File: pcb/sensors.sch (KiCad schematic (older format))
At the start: 2 parts

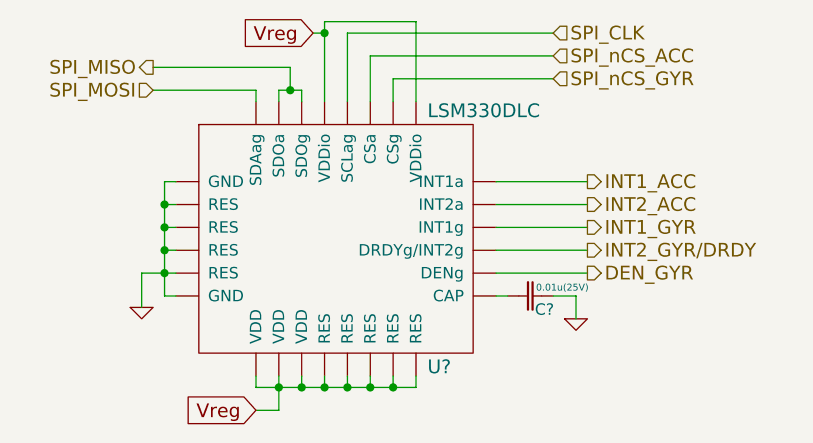
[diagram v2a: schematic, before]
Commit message: Rearranged all the lines except for the power lines.
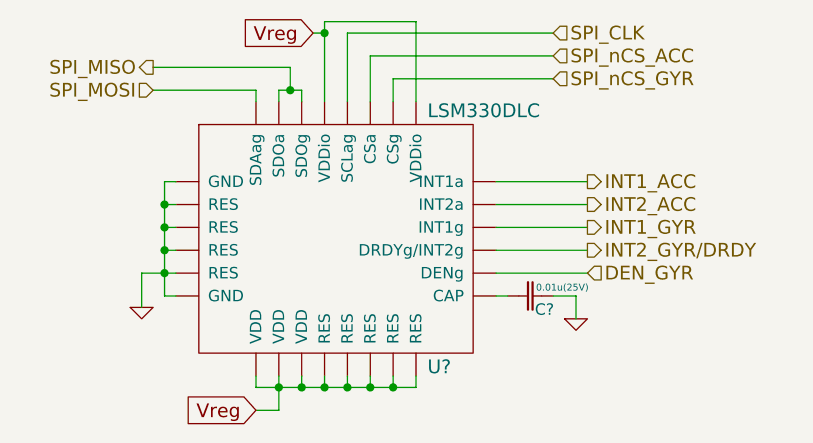
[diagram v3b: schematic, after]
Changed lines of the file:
@@
-EESchema Schematic File Version 2  date 12/16/2012 4:31:25 PM
+EESchema Schematic File Version 2  date 12/17/2012 11:02:29 PM
 LIBS:power
 LIBS:device
@@
 $Descr A4 11700 8267
 encoding utf-8
-Sheet 5 9
+Sheet 2 9
 Title ""
-Date "16 dec 2012"
+Date "18 dec 2012"
 Rev ""
 Comp ""
@@
 Wire Wire Line
 	6600 3900 6200 3900
-Text HLabel 6600 4000 2    60   Output ~ 0
+Text HLabel 6600 4000 2    60   Input ~ 0
 DEN_GYR
 Text HLabel 6600 3900 2    60   Output ~ 0

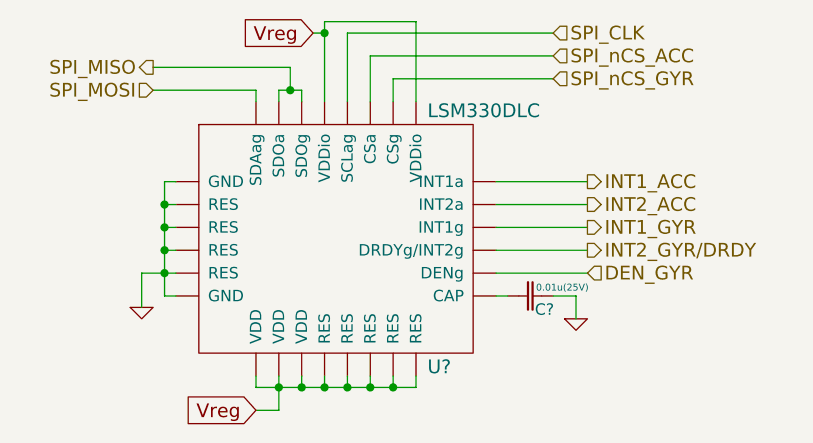
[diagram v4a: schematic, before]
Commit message: Added backlight driver, connected to I2C1, annotated stuff
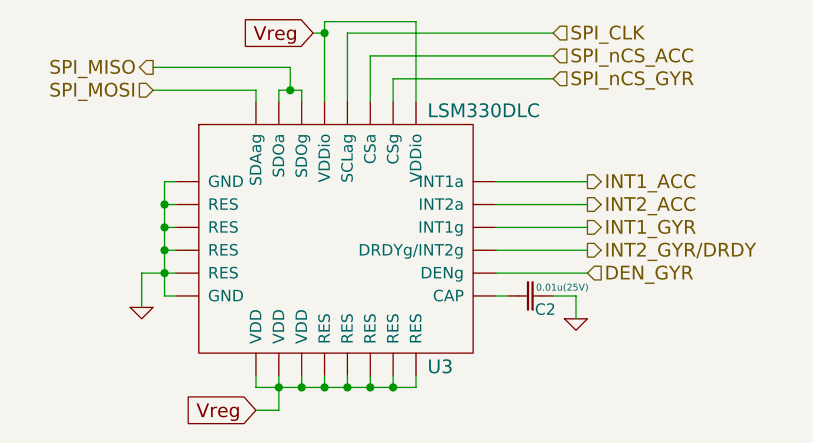
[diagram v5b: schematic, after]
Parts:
- gave numbers to parts that had none: 2
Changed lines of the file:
@@
-EESchema Schematic File Version 2  date 12/19/2012 4:02:29 PM
+EESchema Schematic File Version 2  date Fri 28 Dec 2012 12:18:10 AM EST
 LIBS:power
 LIBS:device
@@
 Sheet 2 9
 Title ""
-Date "19 dec 2012"
+Date "28 dec 2012"
 Rev ""
 Comp ""
@@
 SPI_MISO
 $Comp
-L LSM330DLC U?
+L LSM330DLC U3
 U 1 1 50C11357
 P 5500 3850
-F 0 "U?" H 5900 3325 60  0000 L TNN
+F 0 "U3" H 5900 3325 60  0000 L TNN
 F 1 "LSM330DLC" H 5900 4375 60  0000 L BNN
 	1    5500 3850
@@
 $EndComp
 $Comp
-L GND #PWR?
+L GND #PWR5
 U 1 1 50C11356
 P 4650 4150
-F 0 "#PWR?" H 4650 4150 30  0001 C CNN
+F 0 "#PWR5" H 4650 4150 30  0001 C CNN
 F 1 "GND" H 4650 4080 30  0001 C CNN
 	1    4650 4150
@@
 Vreg
 $Comp
-L CAP C?
+L CAP C2
 U 1 1 50C11355
 P 6350 4100
-F 0 "C?" H 6370 4070 50  0000 L TNN
+F 0 "C2" H 6370 4070 50  0000 L TNN
 F 1 "0.01u(25V)" H 6375 4120 30  0000 L BNN
 	1    6350 4100
@@
 $EndComp
 $Comp
-L GND #PWR?
+L GND #PWR6
 U 1 1 50C11354
 P 6550 4200
-F 0 "#PWR?" H 6550 4200 30  0001 C CNN
+F 0 "#PWR6" H 6550 4200 30  0001 C CNN
 F 1 "GND" H 6550 4130 30  0001 C CNN
 	1    6550 4200

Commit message: Updated netlist on the schematics
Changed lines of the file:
@@
-EESchema Schematic File Version 2  date Mon 07 Jan 2013 11:54:23 AM EST
+EESchema Schematic File Version 2  date 1/8/2013 5:13:17 PM
 LIBS:power
 LIBS:device
@@
 Sheet 2 9
 Title ""
-Date "7 jan 2013"
+Date "8 jan 2013"
 Rev ""
 Comp ""
@@
 	6550 4100 6550 4200
 Wire Wire Line
-	5450 3250 5450 2950
-Wire Wire Line
-	5450 2950 5450 2900
+	5450 3250 5450 2900
 Wire Wire Line
 	5450 2900 5850 2900
@@
 	5850 2900 5850 3250
 Wire Wire Line
-	5250 4450 5250 4500
-Wire Wire Line
-	5250 4500 5250 4600
+	5250 4450 5250 4600
 Wire Wire Line
 	5250 4600 5150 4600
@@
 	4750 3800 4800 3800
 Wire Wire Line
-	4800 3600 4750 3600
-Wire Wire Line
-	4750 3600 4750 3700
-Wire Wire Line
-	4750 3700 4750 3800
-Wire Wire Line
-	4750 3800 4750 3900
-Wire Wire Line
-	4750 3900 4750 4000
-Wire Wire Line
-	4750 4000 4750 4100
+	4750 3600 4800 3600
+Wire Wire Line
+	4750 3600 4750 4100
 Wire Wire Line
 	4750 4100 4800 4100
@@
 	5450 4500 5450 4450
 Wire Wire Line
-	5850 4450 5850 4500
+	5850 4500 5850 4450
 Connection ~ 5650 4500
 Wire Wire Line
-	5850 4500 5750 4500
-Wire Wire Line
-	5750 4500 5650 4500
-Wire Wire Line
-	5650 4500 5550 4500
-Wire Wire Line
-	5550 4500 5450 4500
-Wire Wire Line
-	5450 4500 5350 4500
-Wire Wire Line
-	5350 4500 5250 4500
-Wire Wire Line
-	5250 4500 5150 4500
+	5850 4500 5150 4500
 Wire Wire Line
 	5150 4500 5150 4450
@@
 Connection ~ 4750 3900
 Wire Wire Line
-	4650 4150 4650 4000
-Wire Wire Line
-	4650 4000 4750 4000
-Wire Wire Line
-	4750 4000 4800 4000
-Wire Wire Line
-	5250 3250 5250 3200
-Wire Wire Line
-	5250 3200 5300 3200
-Wire Wire Line
-	5300 3200 5350 3200
+	4650 4000 4650 4150
+Wire Wire Line
+	4800 4000 4650 4000
+Wire Wire Line
+	5250 3200 5250 3250
+Wire Wire Line
+	5250 3200 5350 3200
 Wire Wire Line
 	5350 3200 5350 3250
@@
 $EndComp
 $Comp
-L GND #PWR1
+L GND #PWR01
 U 1 1 50C11356
 P 4650 4150
-F 0 "#PWR1" H 4650 4150 30  0001 C CNN
+F 0 "#PWR01" H 4650 4150 30  0001 C CNN
 F 1 "GND" H 4650 4080 30  0001 C CNN
 	1    4650 4150
@@
 $EndComp
 $Comp
-L GND #PWR2
+L GND #PWR02
 U 1 1 50C11354
 P 6550 4200
-F 0 "#PWR2" H 6550 4200 30  0001 C CNN
+F 0 "#PWR02" H 6550 4200 30  0001 C CNN
 F 1 "GND" H 6550 4130 30  0001 C CNN
 	1    6550 4200

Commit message: Cleaned up antenna symbols and more footprint associations
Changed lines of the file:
@@
-EESchema Schematic File Version 2  date 1/8/2013 5:13:17 PM
+EESchema Schematic File Version 2  date Wed 09 Jan 2013 04:33:42 PM EST
 LIBS:power
 LIBS:device
@@
 Sheet 2 9
 Title ""
-Date "8 jan 2013"
+Date "9 jan 2013"
 Rev ""
 Comp ""
@@
 	4750 3800 4800 3800
 Wire Wire Line
-	4750 3600 4800 3600
+	4800 3600 4750 3600
 Wire Wire Line
 	4750 3600 4750 4100
@@
 	5450 4500 5450 4450
 Wire Wire Line
-	5850 4500 5850 4450
+	5850 4450 5850 4500
 Connection ~ 5650 4500
 Wire Wire Line
@@
 Connection ~ 4750 3900
 Wire Wire Line
-	4650 4000 4650 4150
+	4650 4150 4650 4000
 Wire Wire Line
-	4800 4000 4650 4000
+	4650 4000 4800 4000
 Wire Wire Line
-	5250 3200 5250 3250
+	5250 3250 5250 3200
 Wire Wire Line
 	5250 3200 5350 3200
